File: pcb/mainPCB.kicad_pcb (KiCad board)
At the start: 4 copper layers, 160 x 73.2 mm, 161 parts, among them IC1 FXL6408UMX, IC2 ATA6561-GAQW-N, IC3 ICL3221EIVZ, J1 PTSM-Header-Horizontal-6, J10 Conn_01x08_Female, J11 Conn_01x08_Female, J12 Conn_02x02_Odd_Even, J13 SM04B-SRSS-TB(LF)(SN), J14 USB_B_Micro, J15 RJ45_Amphenol_RJMG1BD3B8K1ANR, J16 DB9_Male_MountingHoles, J17 SM04B-SRSS-TB(LF)(SN), J18 PTSM-Header-Horizontal-2, J3 PTSM-Header-Horizontal-7, J4 CCA-Header-Horizontal-4, J5 PTSM-Header-Horizontal-5, J7 Conn_01x04_Male, J8 Conn_01x04_Male, J9 Conn_01x08_Female, K1 CP1SA-12V-Z, K2 CP1SA-12V-Z, Q1 BC817-40,215, Q2 BC817-40,215, SW1 SW_Push, U1 ESP32-WROOM-32, U10 NUD3124LT1G, U11 LAN8720A, U12 LSM9DS1, U2 AZ1117-3.3, U3 VNH7070AS, U4 ADS1115IDGS, U5 VNH7070AS, U6 PCA9306DCTR, U7 TPD3E001DRLR, U8 CP2102N-A01-GQFN24, U9 VNH7070AS

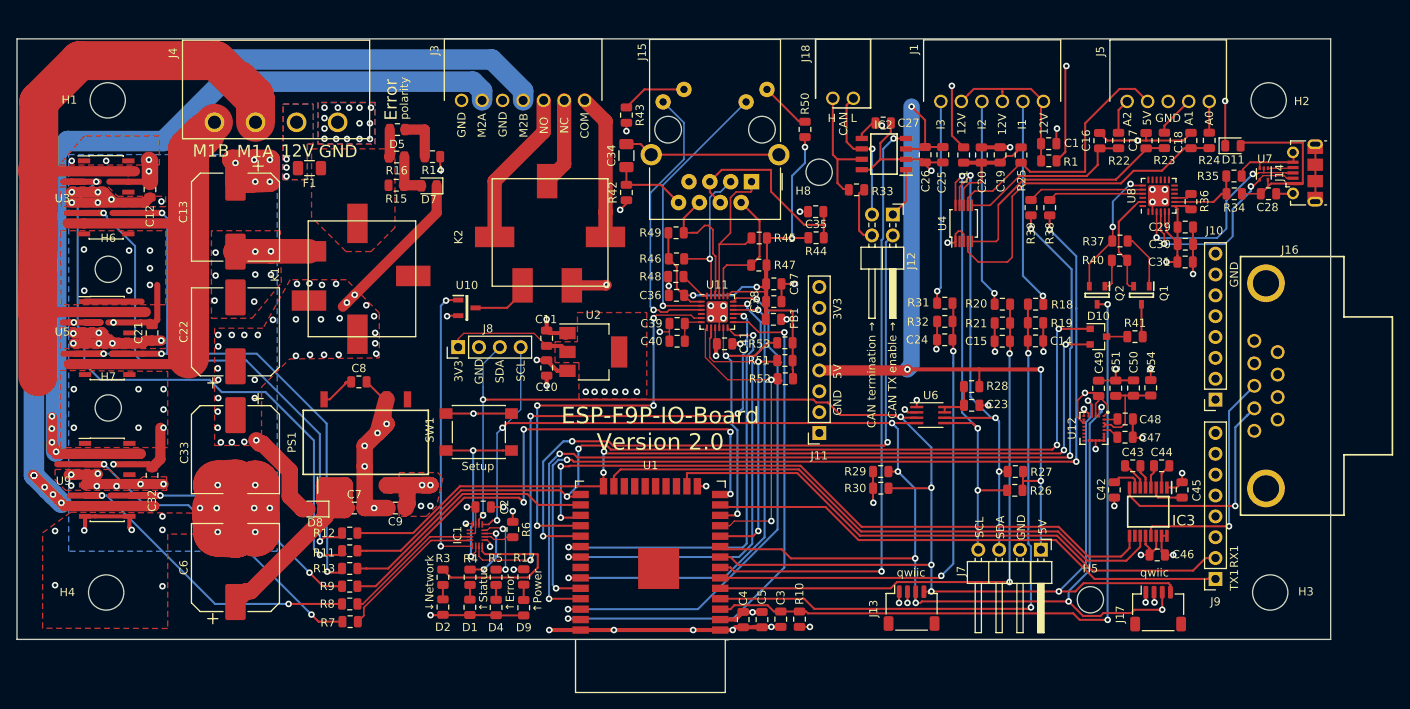
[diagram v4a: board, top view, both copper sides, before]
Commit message: Minor cosmetic changes, Added fiducials. fixes #4
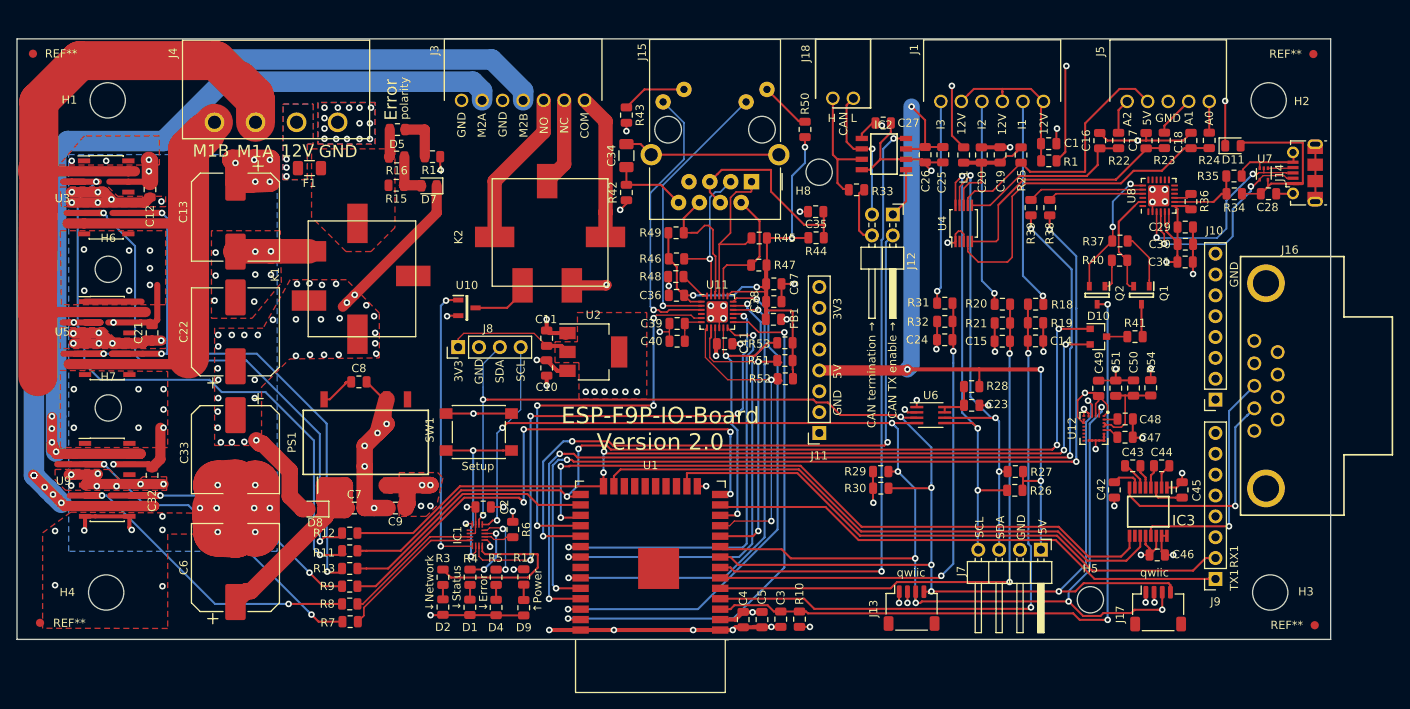
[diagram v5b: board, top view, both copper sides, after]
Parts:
- added REF**: Fiducial_1mm_Dia_2mm_Outer, Fiducial:Fiducial_1mm_Dia_2mm_Outer, F.Cu at (19.4, 39.3)
- added REF**: Fiducial_1mm_Dia_2mm_Outer, Fiducial:Fiducial_1mm_Dia_2mm_Outer, F.Cu at (175.4, 39.3)
- added REF**: Fiducial_1mm_Dia_2mm_Outer, Fiducial:Fiducial_1mm_Dia_2mm_Outer, F.Cu at (175.5, 108.9)
- added REF**: Fiducial_1mm_Dia_2mm_Outer, Fiducial:Fiducial_1mm_Dia_2mm_Outer, F.Cu at (20.3, 108.6)
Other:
- board text added: "↓Error"
- board text added: "↓Status"
- board text removed: "↑Error"
- board text removed: "↑Status"
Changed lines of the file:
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@@
     (tracks 1773)
     (zones 0)
-    (modules 161)
+    (modules 165)
     (nets 181)
   )
@@
     (solder_mask_min_width 0.12)
     (pad_to_paste_clearance -0.01)
-    (aux_axis_origin 146.685 27.305)
+    (aux_axis_origin 17.44472 110.59668)
     (grid_origin 17.44472 110.59668)
     (visible_elements FFFFFF7F)
@@
     )
   )
-  (target plus (at 155.66136 27.85364) (size 5) (width 0.15) (layer Edge.Cuts))
+  (module Fiducial:Fiducial_1mm_Dia_2mm_Outer (layer F.Cu)
+    (at 19.40052 39.27348)
+    (descr "Circular Fiducial, 1mm bare copper top, 2mm keepout (Level A)")
+    (tags fiducial)
+    (attr smd)
+    (fp_text reference REF** (at 3.44424 -0.00508) (layer F.SilkS)
+      (effects (font (size 1 1) (thickness 0.15)))
+    )
+    (fp_text value Fiducial_1mm_Dia_2mm_Outer (at 0 2) (layer F.Fab)
+      (effects (font (size 1 1) (thickness 0.15)))
+    )
+    (fp_circle (center 0 0) (end 1.25 0) (layer F.CrtYd) (width 0.05))
+    (fp_text user %R (at 0 0) (layer F.Fab)
+      (effects (font (size 0.4 0.4) (thickness 0.06)))
+    )
+    (fp_circle (center 0 0) (end 1 0) (layer F.Fab) (width 0.1))
+    (pad "" smd circle (at 0 0) (size 1 1) (layers F.Cu F.Mask)
+      (solder_mask_margin 0.5) (clearance 0.5))
+  )
+  (module Fiducial:Fiducial_1mm_Dia_2mm_Outer (layer F.Cu)
+    (at 175.37176 39.31412)
+    (descr "Circular Fiducial, 1mm bare copper top, 2mm keepout (Level A)")
+    (tags fiducial)
+    (attr smd)
+    (fp_text reference REF** (at -3.39852 -0.00508) (layer F.SilkS)
+      (effects (font (size 1 1) (thickness 0.15)))
+    )
+    (fp_text value Fiducial_1mm_Dia_2mm_Outer (at 0 2) (layer F.Fab)
+      (effects (font (size 1 1) (thickness 0.15)))
+    )
+    (fp_circle (center 0 0) (end 1.25 0) (layer F.CrtYd) (width 0.05))
+    (fp_text user %R (at 0 0) (layer F.Fab)
+      (effects (font (size 0.4 0.4) (thickness 0.06)))
+    )
+    (fp_circle (center 0 0) (end 1 0) (layer F.Fab) (width 0.1))
+    (pad "" smd circle (at 0 0) (size 1 1) (layers F.Cu F.Mask)
+      (solder_mask_margin 0.5) (clearance 0.5))
+  )
+  (module Fiducial:Fiducial_1mm_Dia_2mm_Outer (layer F.Cu)
+    (at 175.5394 108.8898)
+    (descr "Circular Fiducial, 1mm bare copper top, 2mm keepout (Level A)")
+    (tags fiducial)
+    (attr smd)
+    (fp_text reference REF** (at -3.40868 -0.01016) (layer F.SilkS)
+      (effects (font (size 1 1) (thickness 0.15)))
+    )
+    (fp_text value Fiducial_1mm_Dia_2mm_Outer (at 0 2) (layer F.Fab)
+      (effects (font (size 1 1) (thickness 0.15)))
+    )
+    (fp_circle (center 0 0) (end 1.25 0) (layer F.CrtYd) (width 0.05))
+    (fp_text user %R (at 0 0) (layer F.Fab)
+      (effects (font (size 0.4 0.4) (thickness 0.06)))
+    )
+    (fp_circle (center 0 0) (end 1 0) (layer F.Fab) (width 0.1))
+    (pad "" smd circle (at 0 0) (size 1 1) (layers F.Cu F.Mask)
+      (solder_mask_margin 0.5) (clearance 0.5))
+  )
+  (module Fiducial:Fiducial_1mm_Dia_2mm_Outer (layer F.Cu)
+    (at 20.26412 108.60024)
+    (descr "Circular Fiducial, 1mm bare copper top, 2mm keepout (Level A)")
+    (tags fiducial)
+    (attr smd)
+    (fp_text reference REF** (at 3.57124 0.0254) (layer F.SilkS)
+      (effects (font (size 1 1) (thickness 0.15)))
+    )
+    (fp_text value Fiducial_1mm_Dia_2mm_Outer (at 0 2) (layer F.Fab)
+      (effects (font (size 1 1) (thickness 0.15)))
+    )
+    (fp_circle (center 0 0) (end 1.25 0) (layer F.CrtYd) (width 0.05))
+    (fp_text user %R (at 0 0) (layer F.Fab)
+      (effects (font (size 0.4 0.4) (thickness 0.06)))
+    )
+    (fp_circle (center 0 0) (end 1 0) (layer F.Fab) (width 0.1))
+    (pad "" smd circle (at 0 0) (size 1 1) (layers F.Cu F.Mask)
+      (solder_mask_margin 0.5) (clearance 0.5))
+  )
+  (gr_text ↓Error (at 74.2696 104.9274 90) (layer F.SilkS)
+    (effects (font (size 1 1) (thickness 0.2)))
+  )
+  (gr_text ↓Status (at 71.02348 104.34828 90) (layer F.SilkS)
+    (effects (font (size 1 1) (thickness 0.2)))
+  )
+  (target plus (at 81.83372 61.17844) (size 5) (width 0.15) (layer Edge.Cuts))
   (dimension 0.025903 (width 0.3) (layer F.Fab)
     (gr_text "0,026 mm" (at 117.250563 67.275639 281.3099325) (layer F.Fab)
@@
     (effects (font (size 1 1) (thickness 0.2)))
   )
-  (gr_text ↑Status (at 74.2696 104.4956 90) (layer F.SilkS)
-    (effects (font (size 1 1) (thickness 0.2)))
-  )
-  (gr_text ↑Error (at 77.5208 104.9528 90) (layer F.SilkS)
-    (effects (font (size 1 1) (thickness 0.2)))
-  )

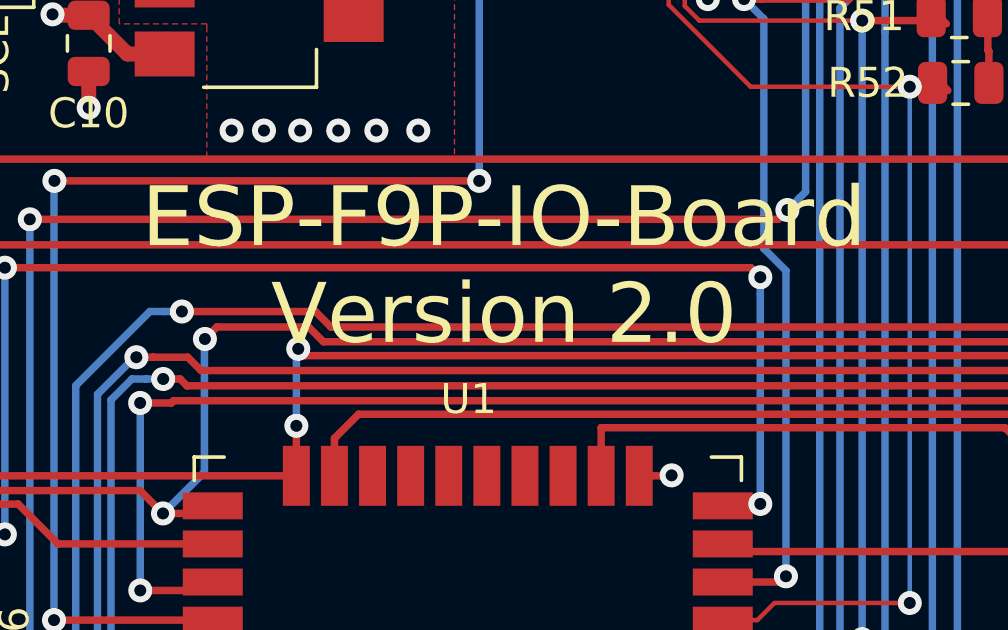
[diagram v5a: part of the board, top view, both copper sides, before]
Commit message: Changed Version on the Board
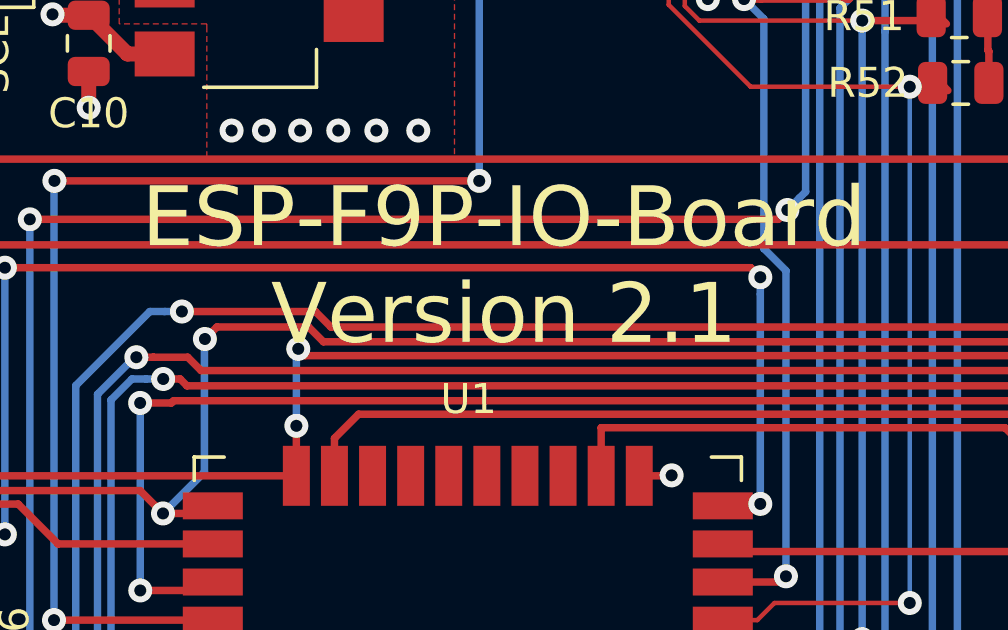
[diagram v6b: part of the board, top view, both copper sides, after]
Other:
- board text added: "ESP-F9P-IO-Board Version 2.1"
- board text removed: "ESP-F9P-IO-Board Version 2.0"
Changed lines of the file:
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@@
     (effects (font (size 1 1) (thickness 0.2)))
   )
-  (gr_text "ESP-F9P-IO-Board\nVersion 2.0" (at 95.8215 84.963) (layer F.SilkS)
+  (gr_text "ESP-F9P-IO-Board\nVersion 2.1" (at 95.8215 84.963) (layer F.SilkS)
     (effects (font (size 2 2) (thickness 0.3)))
   )

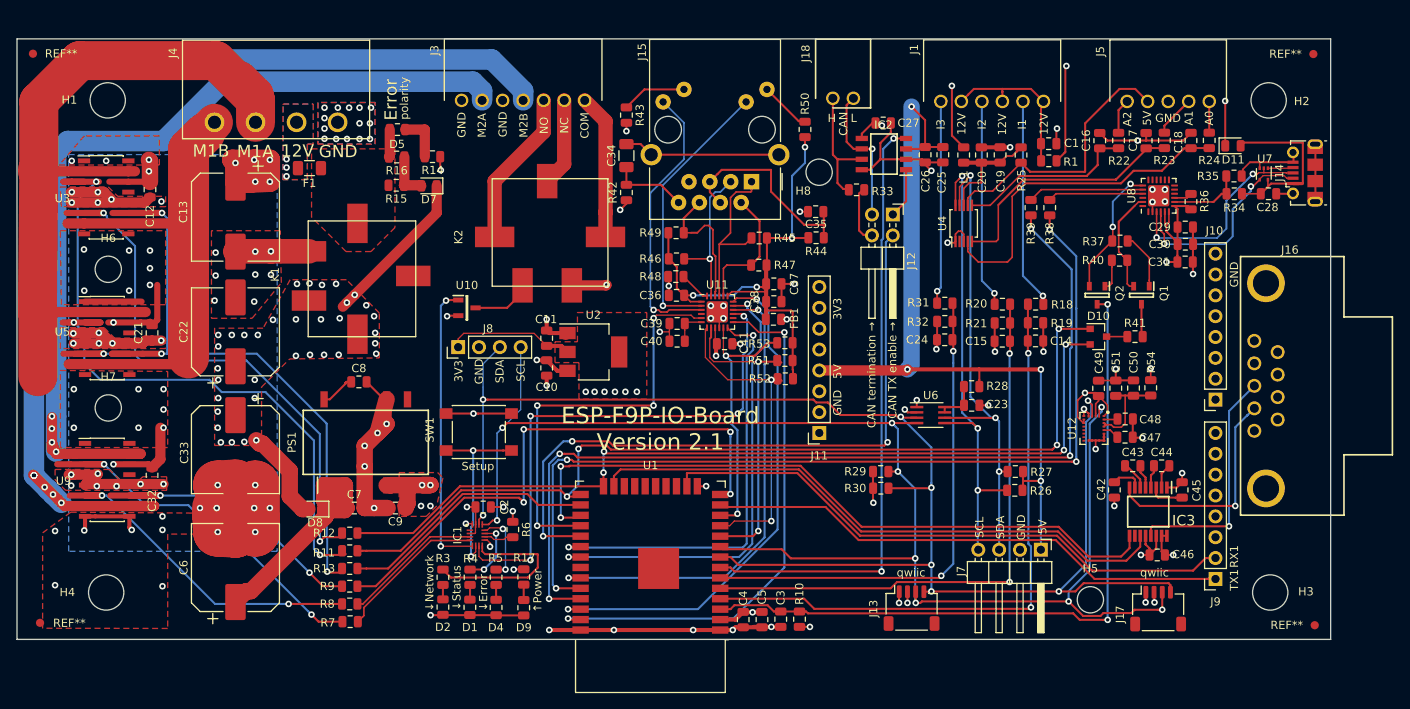
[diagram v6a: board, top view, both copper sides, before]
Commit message: Updated footprints of the SMT connectors, fixes #8. In addition simplified some tracks.
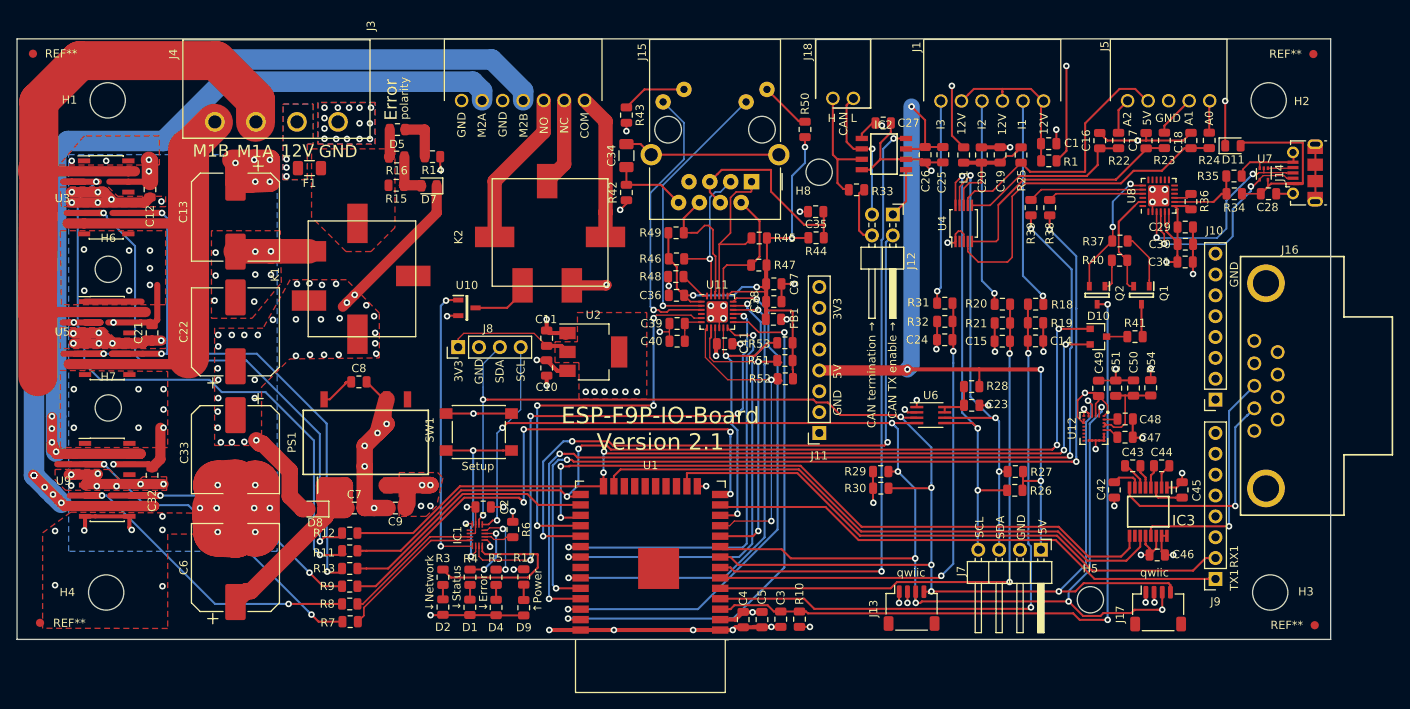
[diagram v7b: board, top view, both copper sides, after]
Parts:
- moved J4 8.73 mm to (49.1, 43.1)
- moved J3 8.30 mm to (78.9, 42.0)
- moved J1 7.44 mm to (136.3, 41.0)
- moved J5 6.02 mm to (157.7, 41.7)
- moved J18 3.66 mm to (118.1, 41.3)
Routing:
- net /motorDriverA/outA: track 97.9 -> 91.9 mm
- net /motorDriverA/outB: track 62.5 -> 59.6 mm
- net +12V: track 114.4 -> 112.6 mm
